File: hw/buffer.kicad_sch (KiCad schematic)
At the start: 13 parts, among them U13 OPA859xDSG

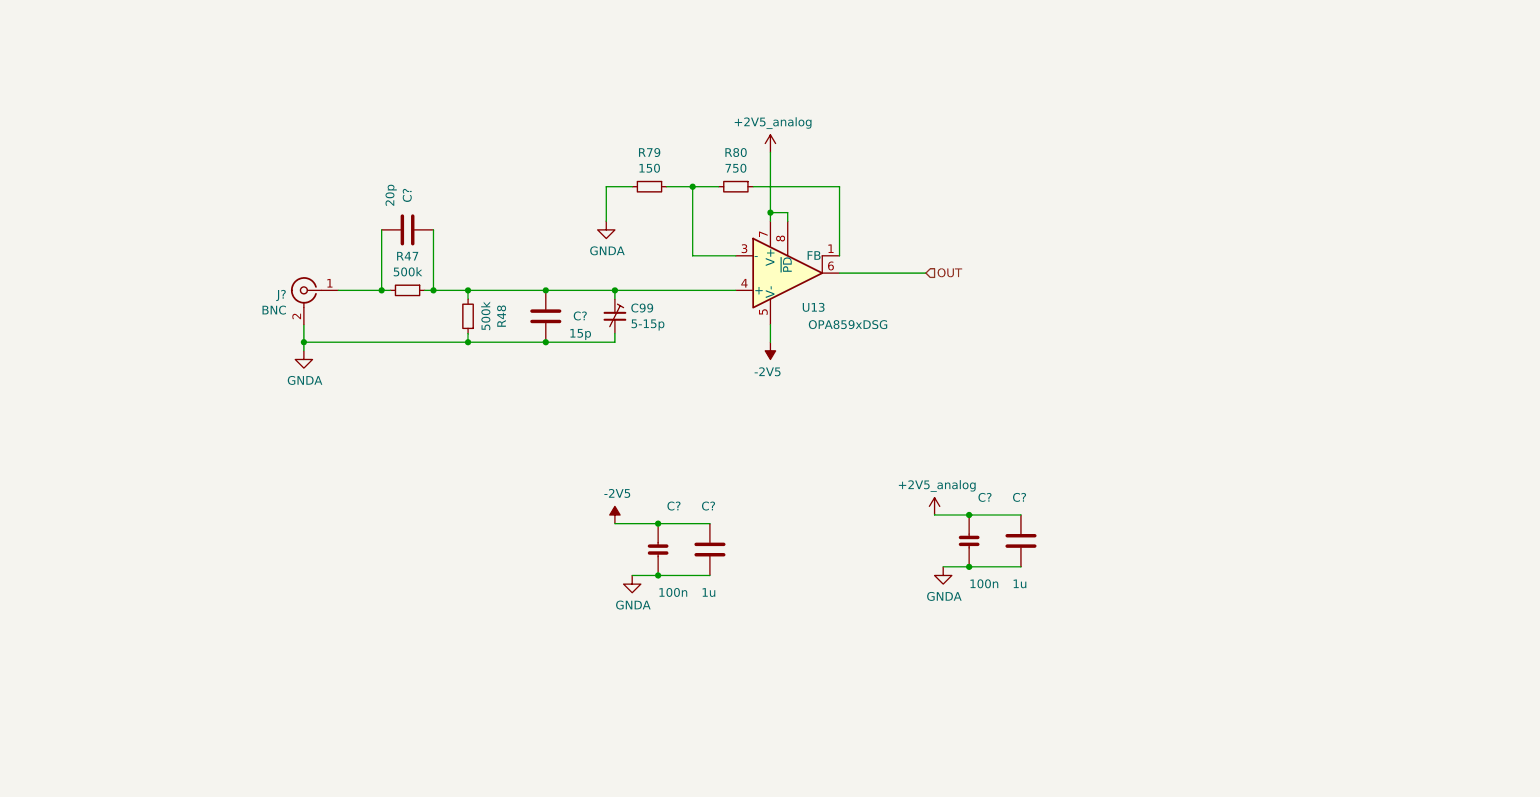
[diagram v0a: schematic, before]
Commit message: basic schematic, started layout (placing first components)
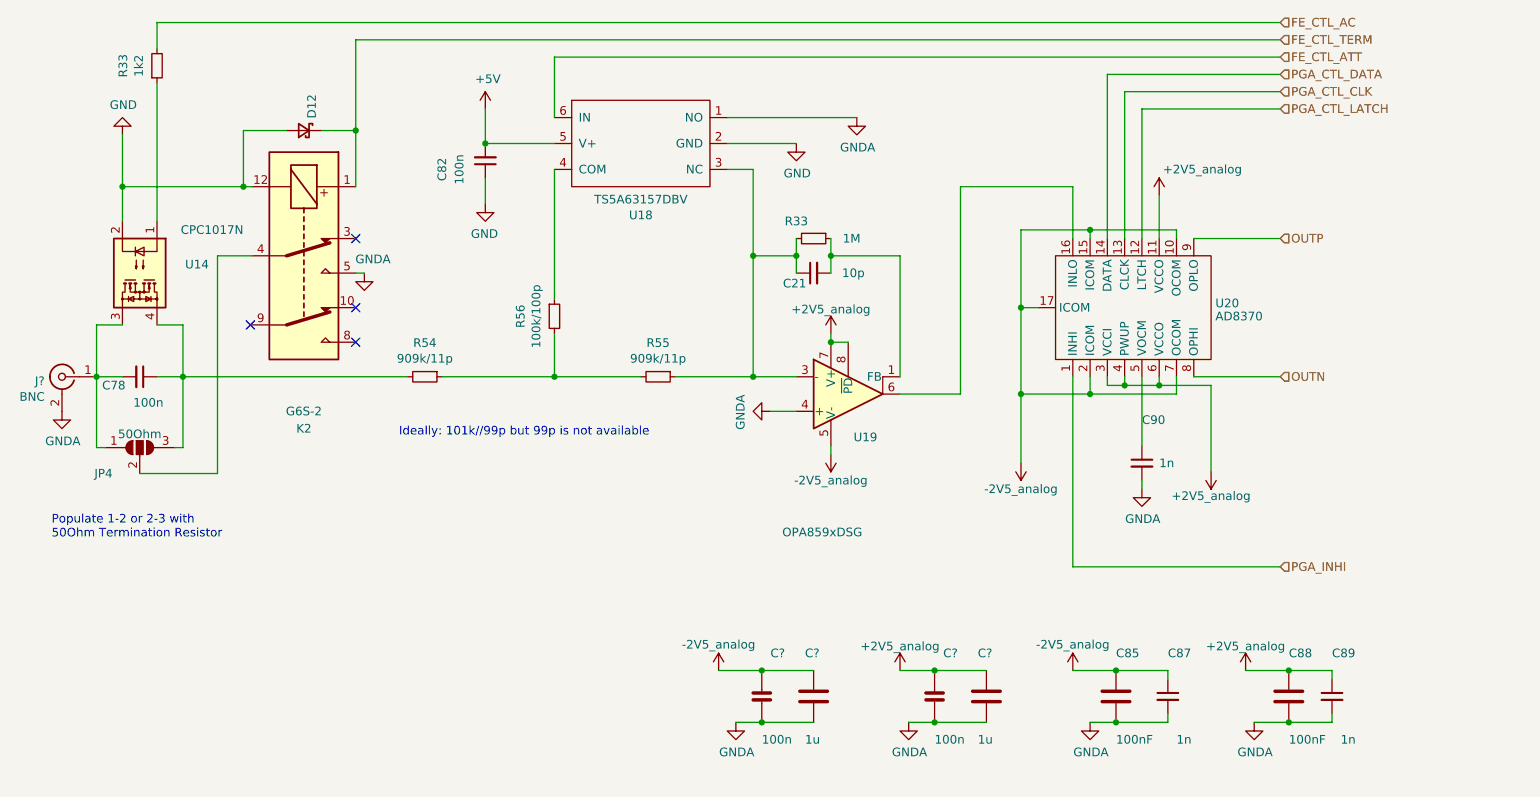
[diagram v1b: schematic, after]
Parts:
- removed C99: 5-15p, proj_footprints:C_Trimmer_EW_Electronics_SCG3S, symbol usbadc-rescue:CTRIM_Small-Device
- removed C?: 15p, Capacitor_SMD:C_0603_1608Metric, symbol fmc:100nF_603
- removed C?: 20p, Capacitor_SMD:C_0603_1608Metric, symbol fmc:100nF_603
- removed R47, R48: 500k, Resistor_SMD:R_0603_1608Metric, symbol Device:R_Small
- removed R79: 150, Resistor_SMD:R_0402_1005Metric, symbol Device:R_Small
- removed R80: 750, Resistor_SMD:R_0402_1005Metric, symbol Device:R_Small
- removed U13: OPA859xDSG, Package_SON:WSON-8-1EP_2x2mm_P0.5mm_EP0.9x1.6mm, symbol Amplifier_Operational:OPA859xDSG
- added C21: 10p, Capacitor_SMD:C_0402_1005Metric, symbol Device:C_Small
- added C78: 100n, Capacitor_SMD:C_0805_2012Metric, symbol Device:C_Small
- added C82: 100n, Capacitor_SMD:C_0603_1608Metric, symbol Device:C_Small
- added C85, C88: 100nF, Capacitor_SMD:C_0603_1608Metric, symbol fmc:100nF_603
- added C87, C89, C90: 1n, Capacitor_SMD:C_0603_1608Metric, symbol Device:C_Small
- added D12: NSR0170HT1G, Diode_SMD:D_SOD-323, symbol Device:D_Schottky_Small
- added JP4: 50Ohm, proj_footprints:J_0603_V, symbol Jumper:SolderJumper_3_Open
- added K2: G6S-2, proj_footprints:TX2SA, symbol Relay:G6S-2
- added R33: 1k2, Resistor_SMD:R_0603_1608Metric, symbol Device:R_Small
- added R33: 1M, Resistor_SMD:R_0402_1005Metric, symbol Device:R_Small
- added R54, R55: 909k/11p, proj_footprints:RC_0603_1608Metric, symbol Device:R_Small
- added R56: 100k/100p, proj_footprints:RC_0603_1608Metric, symbol Device:R_Small
- added U14: CPC1017N, Package_SO:SOP-4_3.8x4.1mm_P2.54mm, symbol Relay_SolidState:CPC1017N
- added U18: TS5A63157DBV, proj_footprints:SOT-23-6_small_cyd, symbol fmc:TS5A3160DBV
- added U19: OPA859xDSG, Package_SON:WSON-8-1EP_2x2mm_P0.5mm_EP0.9x1.6mm, symbol Amplifier_Operational:OPA859xDSG
- added U20: AD8370, Package_SO:TSSOP-16-1EP_4.4x5mm_P0.65mm_EP3x3mm_ThermalVias, symbol fmc:AD8370
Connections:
- net +2V5_analog: now also C88.1, C89.1, U19.7 (V+), U19.8 (~{PD}), U20.11 (VCCO), U20.3 (VCCI), U20.4 (PWUP), U20.6 (VCCO)
- net GNDA: now also C85.2, C87.2, C88.2, C89.2, C90.2, K2.5, U18.1 (NO), U19.4 (+)
- net at J?.1 (In): now also C78.2, JP4.1 (A), U14.3
- net -2V5 renamed -2V5_analog
- net -2V5_analog: now also C85.1, C87.1, U19.5 (V-), U19.9 (V-), U20.10 (OCOM), U20.15 (ICOM), U20.17 (ICOM), U20.2 (ICOM), U20.7 (OCOM)
- new net: C90.1, U20.5 (VOCM)
- new net: R56.1, U18.4 (COM)
- new net: R54.1, R55.2, R56.2
- new net: R33.1, U14.1
- new net: C78.1, JP4.3 (B), R54.2, U14.4
- new net: JP4.2 (C), K2.4
- new net: C21.1, R33.2, R55.1, U18.3 (NC), U19.3 (-)
- new net: C21.2, R33.1, U19.1 (FB)
- new net: U19.6, U20.16 (INLO)
- new net +5V: C82.2, U18.5 (V+)
- new net FE_CTL_AC: R33.2
- new net FE_CTL_ATT: U18.6 (IN)
- new net FE_CTL_TERM: D12.1 (K), K2.1
- new net GND: C82.1, D12.2 (A), K2.12, U14.2, U18.2 (GND)
- new net OUTN: U20.8 (OPHI)
- new net OUTP: U20.9 (OPLO)
- new net PGA_CTL_CLK: U20.13 (CLCK)
- new net PGA_CTL_DATA: U20.14 (DATA)
- new net PGA_CTL_LATCH: U20.12 (LTCH)
- new net PGA_INHI: U20.1 (INHI)
- no-connect marks 0 -> 4
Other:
- note added: "Ideally: 101k//99p but 99p is not available"
- note added: "Populate 1-2 or 2-3 with 50Ohm Termination Resistor"
- moved on the sheet: C?, J?

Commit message: WIP - a lot already laid out.
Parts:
- added C25, C27: 100nF, Capacitor_SMD:C_0603_1608Metric, symbol fmc:100nF_603
- C? (x2): footprint Capacitor_SMD:C_0402_1005Metric -> Capacitor_SMD:C_0603_1608Metric
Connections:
- net +2V5_analog: now also C25.1, C27.1
- net -2V5_analog: now also C25.2, C27.2
- net GNDA: now also K2.4; no longer K2.5
- net at C78.2, J?.1 (In), JP4.1 (A): now also U14.4; no longer U14.3
- net at C78.1, JP4.3 (B), R54.2: now also U14.3; no longer U14.4
- net at JP4.2 (C): now also K2.5; no longer K2.4
- net PGA_INLO: now reaches U20.16 (INLO)
- net PGA_INLO: no longer U19.6
- net +5V renamed Vpp_analog
- new net SE_OUT: U19.6
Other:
- moved on the sheet: R33, U14

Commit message: layout finished (draft)
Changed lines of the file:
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@@
   (junction (at 157.48 144.78) (diameter 0) (color 0 0 0 0)
   )
-  (no_connect (at 82.296 93.98))
+  (no_connect (at 82.55 93.98))
   (no_connect (at 97.79 91.44))
   (no_connect (at 97.79 96.52))

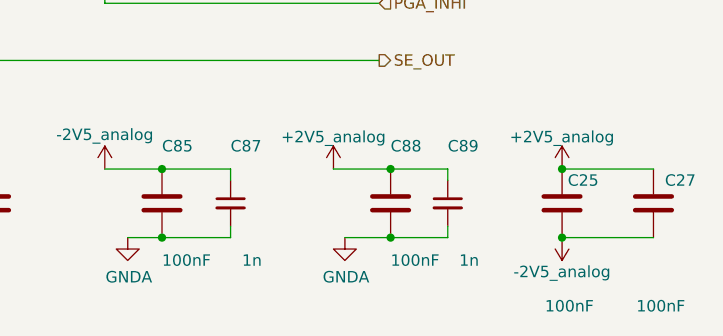
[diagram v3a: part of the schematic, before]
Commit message: finished routing; DRC passes (except for 1 hole violation at push-button)
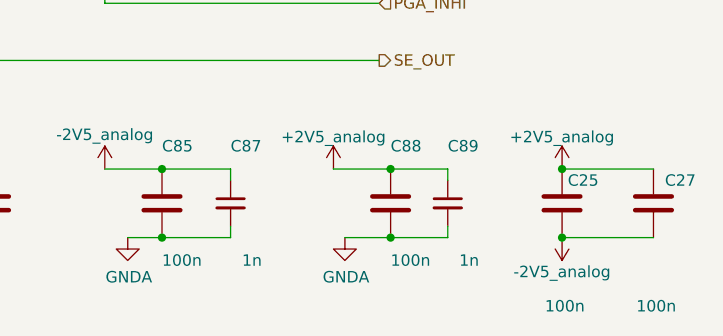
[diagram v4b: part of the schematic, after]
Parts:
- C25, C27, C85, C88: value 100nF -> 100n; Manufacturer Murata -> (none); Part GCJ188R71E104KA12D -> (none)
- C? (x2): Manufacturer Murata -> (none); Part GRM155R61C104KA88D -> (none)
- C? (x2): Manufacturer Murata -> (none); Part GCJ219R71C105KA01 -> (none)
- K2: Manufacturer (none) -> Panasonic; Part (none) -> TX2SA-5V
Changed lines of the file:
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@@
       (effects (font (size 1.27 1.27)) hide)
     )
-    (property "Part" "GRM155R61C104KA88D" (at 186.055 143.51 0)
-      (effects (font (size 1.27 1.27)) hide)
-    )
-    (property "Manufacturer" "Murata" (at 188.595 140.97 0)
+    (property "Part" "" (at 186.055 143.51 0)
+      (effects (font (size 1.27 1.27)) hide)
+    )
+    (property "Manufacturer" "" (at 188.595 140.97 0)
       (effects (font (size 1.27 1.27)) hide)
     )
@@
       (effects (font (size 1.27 1.27)) hide)
     )
-    (property "Part" "GCJ219R71C105KA01" (at 193.675 143.51 0)
-      (effects (font (size 1.27 1.27)) hide)
-    )
-    (property "Manufacturer" "Murata" (at 196.215 140.97 0)
+    (property "Part" "" (at 193.675 143.51 0)
+      (effects (font (size 1.27 1.27)) hide)
+    )
+    (property "Manufacturer" "" (at 196.215 140.97 0)
       (effects (font (size 1.27 1.27)) hide)
     )
@@
       (effects (font (size 1.27 1.27)) hide)
     )
-    (property "Part" "GRM155R61C104KA88D" (at 160.655 143.51 0)
-      (effects (font (size 1.27 1.27)) hide)
-    )
-    (property "Manufacturer" "Murata" (at 163.195 140.97 0)
+    (property "Part" "" (at 160.655 143.51 0)
+      (effects (font (size 1.27 1.27)) hide)
+    )
+    (property "Manufacturer" "" (at 163.195 140.97 0)
       (effects (font (size 1.27 1.27)) hide)
     )
@@
       (effects (font (size 1.27 1.27)) hide)
     )
-    (property "Part" "GCJ219R71C105KA01" (at 168.275 143.51 0)
-      (effects (font (size 1.27 1.27)) hide)
-    )
-    (property "Manufacturer" "Murata" (at 170.815 140.97 0)
+    (property "Part" "" (at 168.275 143.51 0)
+      (effects (font (size 1.27 1.27)) hide)
+    )
+    (property "Manufacturer" "" (at 170.815 140.97 0)
       (effects (font (size 1.27 1.27)) hide)
     )
@@
       (effects (font (size 1.27 1.27)) (justify left))
     )
-    (property "Value" "100nF" (at 262.255 160.02 0)
+    (property "Value" "100n" (at 262.255 160.02 0)
       (effects (font (size 1.27 1.27)) (justify left))
     )
@@
       (effects (font (size 1.27 1.27)) hide)
     )
-    (property "Part" "GCJ188R71E104KA12D" (at 267.335 143.51 0)
-      (effects (font (size 1.27 1.27)) hide)
-    )
-    (property "Manufacturer" "Murata" (at 269.875 140.97 0)
+    (property "Part" "" (at 267.335 143.51 0)
+      (effects (font (size 1.27 1.27)) hide)
+    )
+    (property "Manufacturer" "" (at 269.875 140.97 0)
       (effects (font (size 1.27 1.27)) hide)
     )
@@
       (effects (font (size 1.27 1.27)) (justify left))
     )
-    (property "Value" "100nF" (at 252.095 160.02 0)
+    (property "Value" "100n" (at 252.095 160.02 0)
       (effects (font (size 1.27 1.27)) (justify left))
     )
@@
       (effects (font (size 1.27 1.27)) hide)
     )
-    (property "Part" "GCJ188R71E104KA12D" (at 257.175 143.51 0)
-      (effects (font (size 1.27 1.27)) hide)
-    )
-    (property "Manufacturer" "Murata" (at 259.715 140.97 0)
+    (property "Part" "" (at 257.175 143.51 0)
+      (effects (font (size 1.27 1.27)) hide)
+    )
+    (property "Manufacturer" "" (at 259.715 140.97 0)
       (effects (font (size 1.27 1.27)) hide)
     )
@@
     )
     (property "Datasheet" "http://omronfs.omron.com/en_US/ecb/products/pdf/en-g6s.pdf" (at 90.17 83.82 0)
+      (effects (font (size 1.27 1.27)) hide)
+    )
+    (property "Part" "TX2SA-5V" (at 90.17 83.82 90)
+      (effects (font (size 1.27 1.27)) hide)
+    )
+    (property "Manufacturer" "Panasonic" (at 90.17 83.82 90)
       (effects (font (size 1.27 1.27)) hide)
     )
@@
       (effects (font (size 1.27 1.27)) (justify left))
     )
-    (property "Value" "100nF" (at 234.95 154.94 0)
+    (property "Value" "100n" (at 234.95 154.94 0)
       (effects (font (size 1.27 1.27)) (justify left))
     )
@@
       (effects (font (size 1.27 1.27)) hide)
     )
-    (property "Part" "GCJ188R71E104KA12D" (at 238.125 143.51 0)
-      (effects (font (size 1.27 1.27)) hide)
-    )
-    (property "Manufacturer" "Murata" (at 240.665 140.97 0)
+    (property "Part" "" (at 238.125 143.51 0)
+      (effects (font (size 1.27 1.27)) hide)
+    )
+    (property "Manufacturer" "" (at 240.665 140.97 0)
       (effects (font (size 1.27 1.27)) hide)
     )
@@
       (effects (font (size 1.27 1.27)) (justify left))
     )
-    (property "Value" "100nF" (at 209.55 154.94 0)
+    (property "Value" "100n" (at 209.55 154.94 0)
       (effects (font (size 1.27 1.27)) (justify left))
     )
@@
       (effects (font (size 1.27 1.27)) hide)
     )
-    (property "Part" "GCJ188R71E104KA12D" (at 212.725 143.51 0)
-      (effects (font (size 1.27 1.27)) hide)
-    )
-    (property "Manufacturer" "Murata" (at 215.265 140.97 0)
-      (effects (font (size 1.27 1.27)) hide)
-    )
+    (property "Part" "" (at 212.725 143.51 0)
+      (effects (font (size 1.27 1.27)) hide)
+    )
+    (property "Manufacturer" "" (at 215.265 140.97 0)
+      (effects (font (size 1.27 1.27)) hide)
+    )

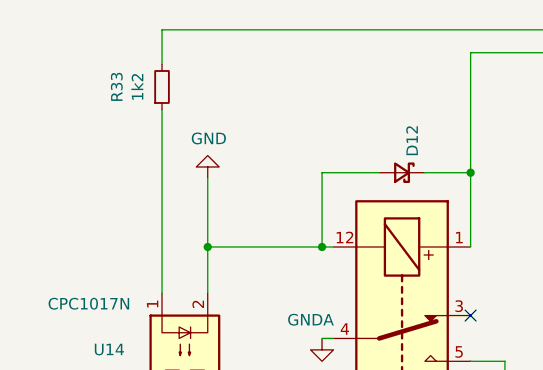
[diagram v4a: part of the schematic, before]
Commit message: standardized resistor/capacitor values
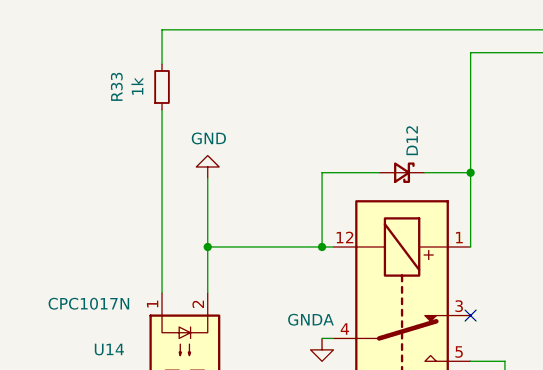
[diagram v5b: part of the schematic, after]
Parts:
- R33: value 1k2 -> 1k
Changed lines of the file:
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@@
       (effects (font (size 1.27 1.27)))
     )
-    (property "Value" "1k2" (at 60.833 55.88 90)
+    (property "Value" "1k" (at 60.833 55.88 90)
       (effects (font (size 1.27 1.27)))
     )

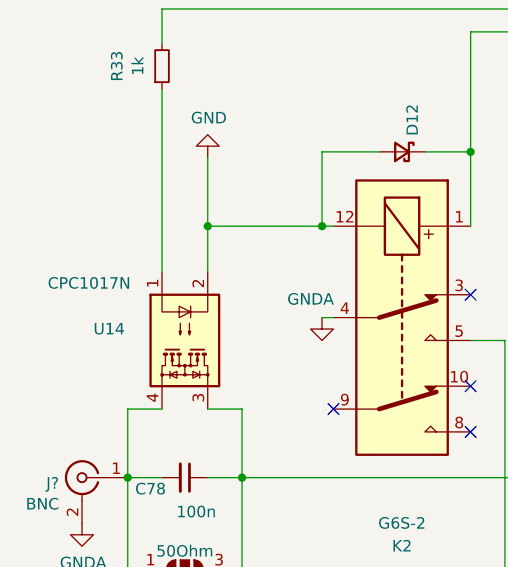
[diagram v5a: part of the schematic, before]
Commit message: buffer.kicad_sch: updated part number of solid-state relay
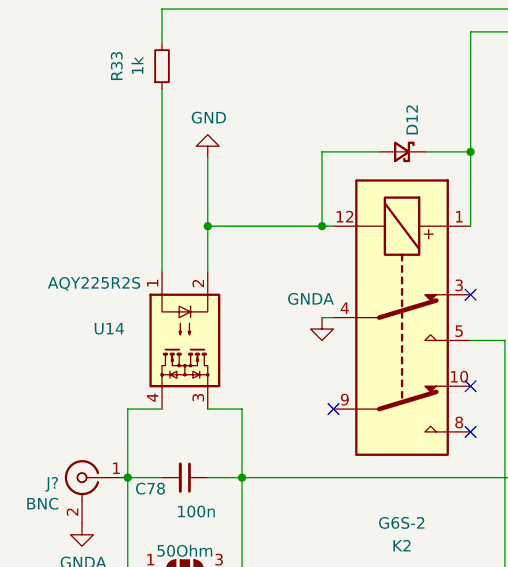
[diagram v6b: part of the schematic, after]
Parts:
- U14: value CPC1017N -> AQY225R2S
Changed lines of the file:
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@@
       (effects (font (size 1.27 1.27)) (justify right))
     )
-    (property "Value" "CPC1017N" (at 50.8 80.01 90)
+    (property "Value" "AQY225R2S" (at 50.8 80.01 90)
       (effects (font (size 1.27 1.27)) (justify right))
     )
